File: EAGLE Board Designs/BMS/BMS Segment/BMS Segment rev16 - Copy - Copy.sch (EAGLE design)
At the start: 140 parts, among them J0 CONNECTOR-1_5222_, J1 CONNECTOR-1_5222_, J10 CONNECTOR-1_5222_, J11 CONNECTOR-1_5222_, J12 CONNECTOR-1_5222_, J13 CONNECTOR-1_5222_, J14 CONNECTOR-1_5222_, J15 CONNECTOR-1_5222_, J16 CONNECTOR-1_5222_, J17 CONNECTOR-1_5222_, J18 CONNECTOR-1_5222_, J2 CONNECTOR-1_5222_, J27 CONNECTOR-2_NANOFIT_SMD_VERTI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, J28 CONNECTOR-2_NANOFIT_SMD_VERTI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, J29 CONNECTOR-1_5222_, J3 CONNECTOR-1_5222_, J30 CONNECTOR-1_5222_, J31 CONNECTOR-1_5222_, J32 CONNECTOR-2_NANOFIT_SMD_VERTI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, J33 CONNECTOR-2_NANOFIT_SMD_VERTI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, J34 CONNECTOR-2_NANOFIT_SMD_VERTI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, J35 CONNECTOR-2_NANOFIT_SMD_VERTI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, J37 CONNECTOR-2_NANOFIT_SMD_VERTI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, J38 CONNECTOR-2_NANOFIT_SMD_VERTI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, J39 CONNECTOR-2_NANOFIT_SMD_VERTI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, J4 CONNECTOR-1_5222_, J40 CONNECTOR-2_NANOFIT_SMD_VERTI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, J5 CONNECTOR-1_5222_, J6 CONNECTOR-1_5222_, J7 CONNECTOR-1_5222_, J8 CONNECTOR-1_5222_, J9 CONNECTOR-1_5222_, Q1 TRANSISTOR_NPN, Q2 TRANSISTOR_NPN, T1 TRANSFORMER_HM2112ZNLT, T2 TRANSFORMER_HM2112ZNLT, U1 LTC6811-2, U2 LTC6811-2

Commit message: Reviewed the schematic and made changes to make it look better
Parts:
- removed CELL0.C1: CAPACITOR_0603_100V_10NF, HyTechDevices:CAPACITOR_0603_100V_10NF
- removed R51: RESISTOR_0603_100, HyTechDevices:RESISTOR_0603_100
- added C7: CAPACITOR_0603_100V_10NF, HyTechDevices:CAPACITOR_0603_100V_10NF
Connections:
- net C0_A renamed N$91
- removed net C0: CELL0.C1.1, CELL0.R1.2, U2.C0
- removed net N$15 (its old number): R28.2, U1.IBIAS
- removed net N$20 (its old number): U1.C2
- new net N$61: R27.2, R28.2, U1.ICMP
- new net N$89: C7.1, CELL0.R1.2, U2.C0
- new net N$9: U1.S9
- new net V-_L: C7.2, R29.1, U2.V-
- new net V-_U: C14.2, R27.1, U1.V-
- net N$28: no longer R51.1
- net N$7: now also U1.C2; no longer U1.S9
- net N$70: now also U1.IBIAS; no longer R27.2, U1.ICMP
- net N$85: no longer R51.2
- net SENSE_12: no longer R24.1
- net SENSE_21: now also SENSE18.R1.1; no longer SENSE18.R1.2
- net V+: now also SENSE18.R1.2; no longer SENSE18.R1.1
- net V+B: now also R24.1; no longer R24.2
- net V-: no longer CELL0.C1.2, R29.1, U2.V-
- net V-B: now also R24.2; no longer C14.2, R27.1, U1.V-
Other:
- moved on the sheet: C1, C10, C11, C12, C13, C14, C2, C26, C28, C3, C4, C5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

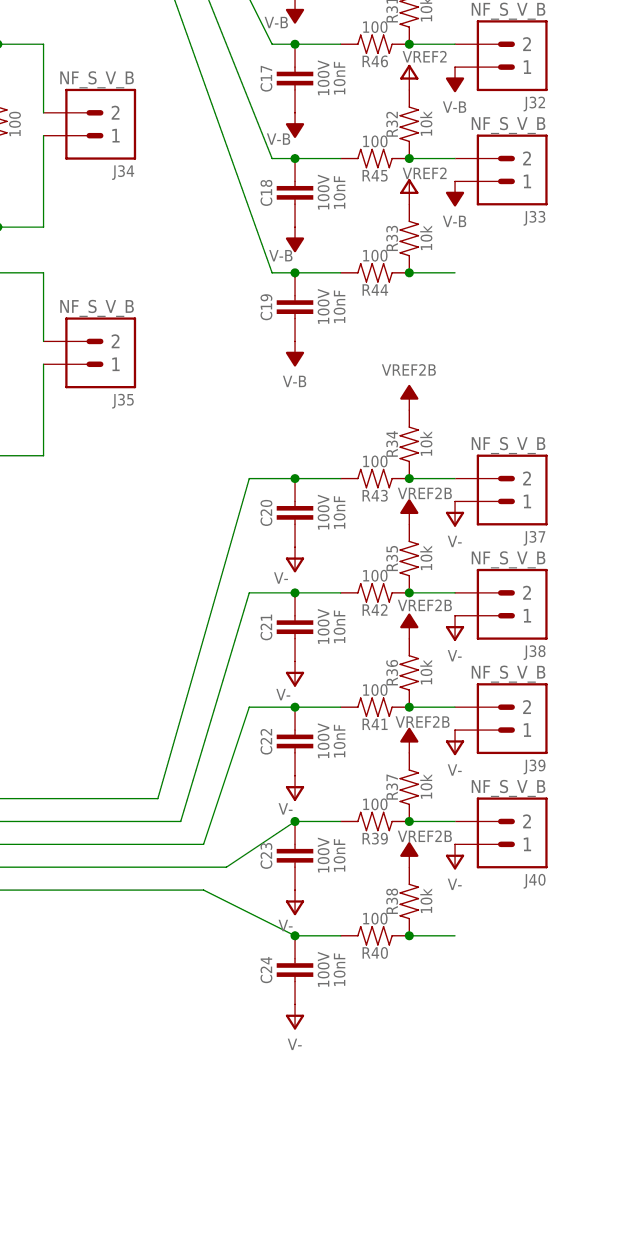
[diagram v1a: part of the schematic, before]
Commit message: changed the resister, added humidity sensor
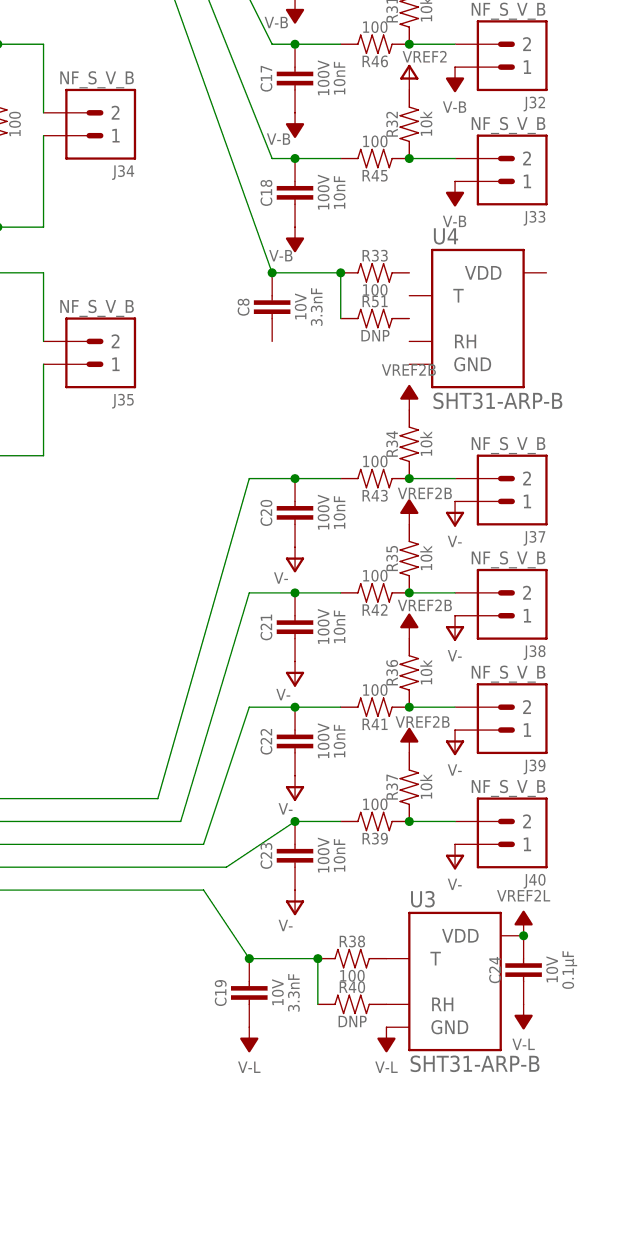
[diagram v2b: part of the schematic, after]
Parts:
- removed R44: RESISTOR_0603_100, HyTechDevices:RESISTOR_0603_100
- added C8: CAPACITOR_0603_10V_3.3NF, HyTechDevices:CAPACITOR_0603_10V_3.3NF
- added R51: RESISTOR_0603_DNP, HyTechDevices:RESISTOR_0603_DNP
- added U3, U4: SHT31-ARP-B, HyTechDevices:SHT31-ARP-B
- C19: value CAPACITOR_0603_100V_10NF -> CAPACITOR_0603_10V_3.3NF; device HyTechDevices:CAPACITOR_0603_100V_10NF -> HyTechDevices:CAPACITOR_0603_10V_3.3NF
- C24: value CAPACITOR_0603_100V_10NF -> CAPACITOR_0603_10V_0.1UF; device HyTechDevices:CAPACITOR_0603_100V_10NF -> HyTechDevices:CAPACITOR_0603_10V_0.1UF
- R33, R38: value RESISTOR_0603_10K -> RESISTOR_0603_100; device HyTechDevices:RESISTOR_0603_10K -> HyTechDevices:RESISTOR_0603_100
- R40: value RESISTOR_0603_100 -> RESISTOR_0603_DNP; device HyTechDevices:RESISTOR_0603_100 -> HyTechDevices:RESISTOR_0603_DNP
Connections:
- new net V-L: C19.2, C24.2, U3.GND
- new net VREF2L: C24.1, U3.VDD
- net N$75: now also C19.1, R38.1, R40.1; no longer C24.1, R40.2
- net N$81: now also R40.2, U3.RH; no longer R33.1, R44.1
- net N$82: now also C8.1, R33.1, R51.1; no longer C19.1, R44.2
- net N$83: now also R38.2, U3.T; no longer R38.1, R40.1
- net V-: no longer C24.2
- net V-B: no longer C19.2
- net VREF2: no longer R33.2
- net VREF2B: no longer R38.2
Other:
- note added: "page 70 rc filter 1k gate resister ltc6811-2 demo circuit"
- moved on the sheet: C19, C24, R33, R38, R40

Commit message: Added correct connectors, added a better description, made the text all proportional, made the schem look better
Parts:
- added C25: CAPACITOR_0603_10V_0.1UF, HyTechDevices:CAPACITOR_0603_10V_0.1UF
- J27, J28, J32, J33, J34, J35, J37, J38, J39, J40: value CONNECTOR-2_NANOFIT_SMD_VERTICAL_BLACK -> CONNECTOR-2_MICROFIT_SMD_RIGHTANGLE_02_SINGLE_BLACK; device HyTechDevices:CONNECTOR-2_NANOFIT_SMD_VERTICAL_BLACK -> HyTechDevices:CONNECTOR-2_MICROFIT_SMD_RIGHTANGLE_02_SINGLE_BLACK
- renumbered CELL0.R1 to R53, SENSE18.R1 to R44
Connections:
- net N$26 renamed SENSE20
- net N$27 renamed SENSE19
- new net N$12: R51.2, U4.RH
- new net N$30: R33.2, U4.T
- new net SENSE0: F0.2, R53.1
- new net SENSE12: F12.2, R24.2, R3.1
- new net SENSE21: F21.2, R44.1
- new net V-U: C25.2, C8.2, U4.GND
- new net VREF2U: C25.1, U4.VDD
- net SENSE_21: no longer F21.2, R44.1
- net V-: no longer F0.2, R53.1
- net V-B: no longer F12.2, R24.2, R3.1
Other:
- note added: "RC Filter Determined by one shown on page 70 of the datasheet. 1k gate resister for the mosfet determined by the ltc6811-2 demo circuit."
- note removed: "page 70 rc filter 1k gate resister ltc6811-2 demo circuit"
- moved on the sheet: C15, C16, C17, C18, C19, C20, C21, C22, C23, C8, F12, F13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
